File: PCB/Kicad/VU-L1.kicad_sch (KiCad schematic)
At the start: 32 parts, among them U1 SR1-L1, U2 SR2-L1

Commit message: PDF
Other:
- note added: "VU LINE 1"
- moved on the sheet: D16, D17, D18, D19, D20, D21, D22, D23, D24, D25, D26, D27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

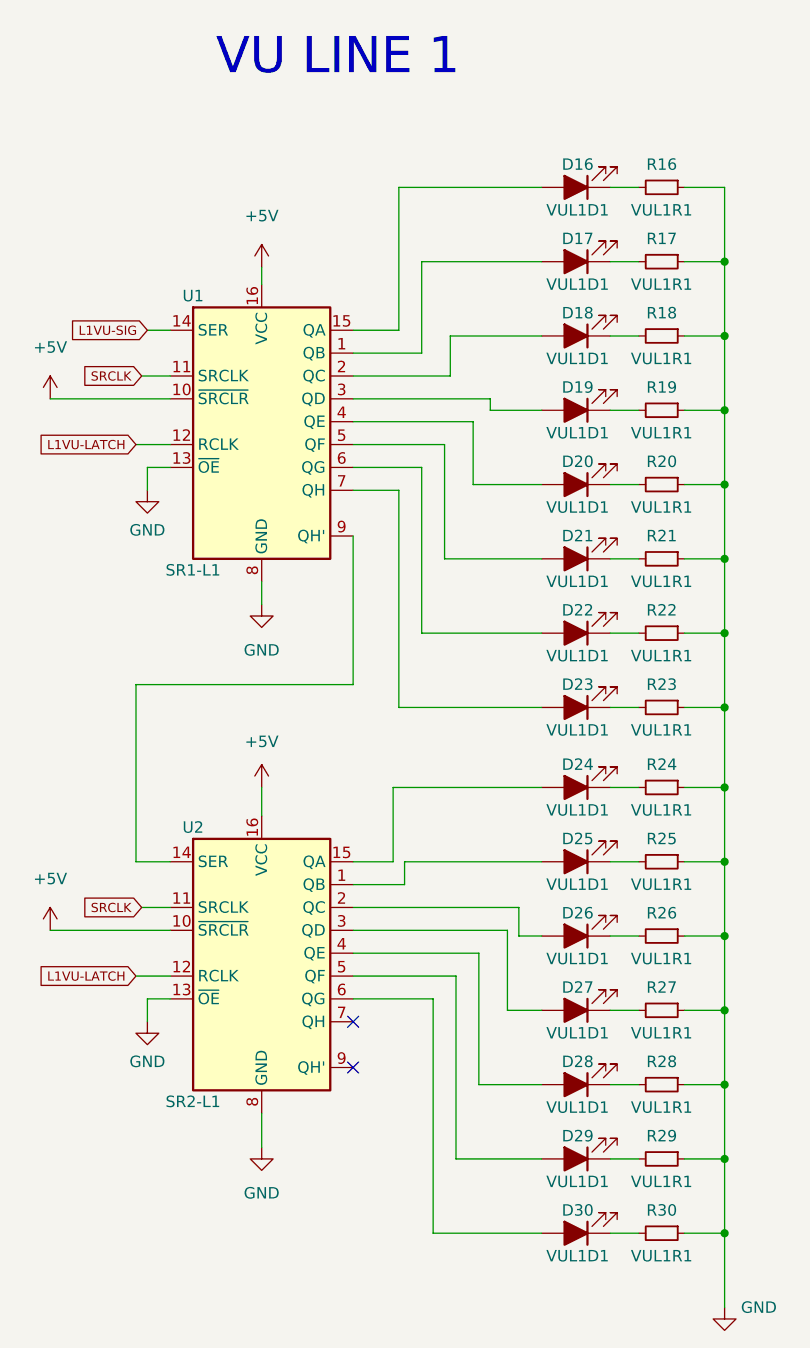
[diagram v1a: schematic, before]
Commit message: added transistor and 3x leds play- cue
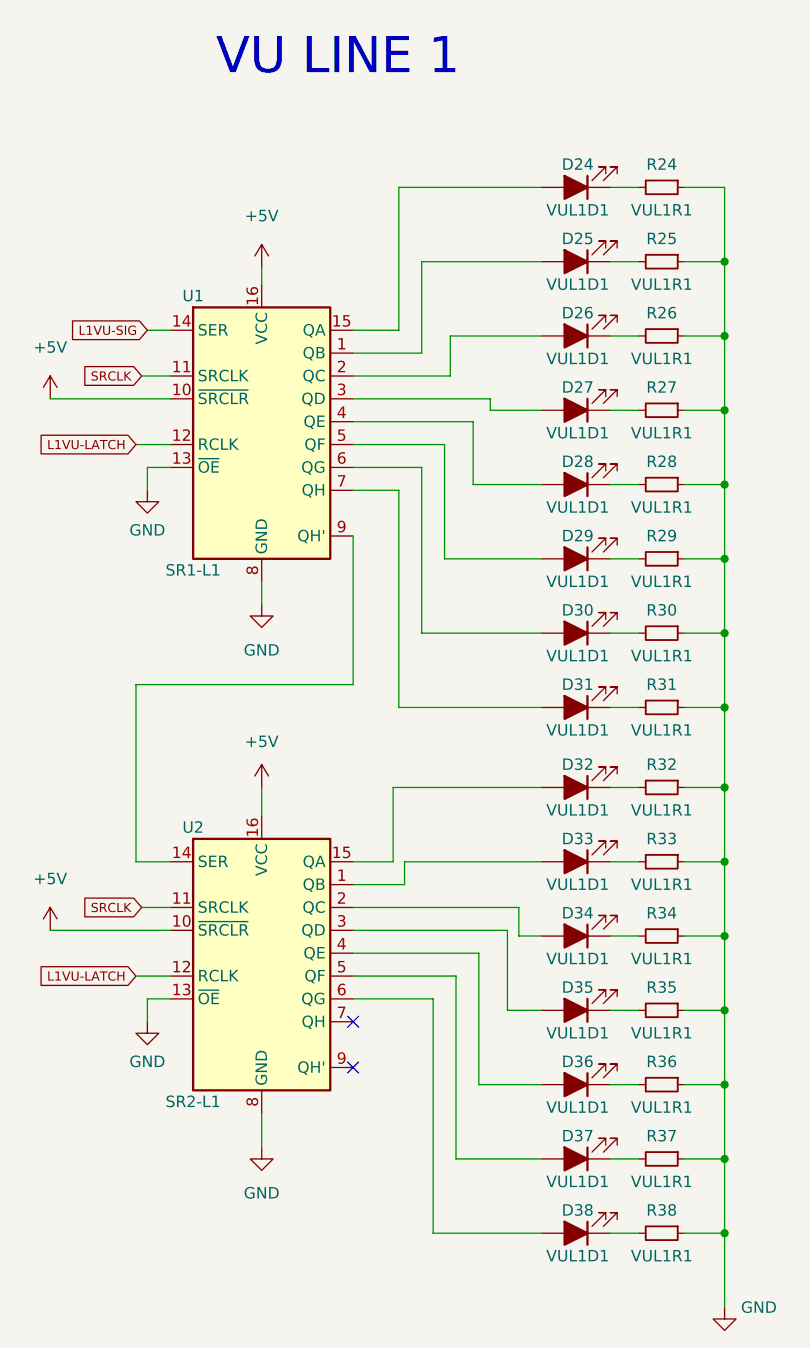
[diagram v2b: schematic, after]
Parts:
- U1, U2: footprint (none) -> Library:SO-16_3.9x9.9mm_P1.27mm
- renumbered D16 to D24, D17 to D25, D18 to D26, D19 to D27, D20 to D28, D21 to D29, D22 to D30, D23 to D31, D24 to D32, D25 to D33, D26 to D34, D27 to D35, D28 to D36, D29 to D37, D30 to D38, R16 to R24, R17 to R25, R18 to R26, R19 to R27, R20 to R28, R21 to R29, R22 to R30, R23 to R31, R24 to R32, R25 to R33, R26 to R34, R27 to R35, R28 to R36, R29 to R37, R30 to R38

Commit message: routing WIP
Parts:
- D33, D34, D35, D36: footprint Library:LED_GREEN -> Library:LED_YELLOW
- D37, D38: footprint Library:LED_GREEN -> Library:LED_RED
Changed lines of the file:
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@@
     (property "Reference" "D33" (id 0) (at 122.7455 115.57 0))
     (property "Value" "VUL1D1" (id 1) (at 122.7455 120.65 0))
-    (property "Footprint" "Library:LED_GREEN" (id 2) (at 122.555 118.11 0)
+    (property "Footprint" "Library:LED_YELLOW" (id 2) (at 122.555 118.11 0)
       (effects (font (size 1.27 1.27)) hide)
     )
@@
     (property "Reference" "D34" (id 0) (at 122.7455 123.825 0))
     (property "Value" "VUL1D1" (id 1) (at 122.7455 128.905 0))
-    (property "Footprint" "Library:LED_GREEN" (id 2) (at 122.555 126.365 0)
+    (property "Footprint" "Library:LED_YELLOW" (id 2) (at 122.555 126.365 0)
       (effects (font (size 1.27 1.27)) hide)
     )
@@
     (property "Reference" "D35" (id 0) (at 122.7455 132.08 0))
     (property "Value" "VUL1D1" (id 1) (at 122.7455 137.16 0))
-    (property "Footprint" "Library:LED_GREEN" (id 2) (at 122.555 134.62 0)
+    (property "Footprint" "Library:LED_YELLOW" (id 2) (at 122.555 134.62 0)
       (effects (font (size 1.27 1.27)) hide)
     )
@@
     (property "Reference" "D36" (id 0) (at 122.7455 140.335 0))
     (property "Value" "VUL1D1" (id 1) (at 122.7455 145.415 0))
-    (property "Footprint" "Library:LED_GREEN" (id 2) (at 122.555 142.875 0)
+    (property "Footprint" "Library:LED_YELLOW" (id 2) (at 122.555 142.875 0)
       (effects (font (size 1.27 1.27)) hide)
     )
@@
     (property "Reference" "D37" (id 0) (at 122.7455 148.59 0))
     (property "Value" "VUL1D1" (id 1) (at 122.7455 153.67 0))
-    (property "Footprint" "Library:LED_GREEN" (id 2) (at 122.555 151.13 0)
+    (property "Footprint" "Library:LED_RED" (id 2) (at 122.555 151.13 0)
       (effects (font (size 1.27 1.27)) hide)
     )
@@
     (property "Reference" "D38" (id 0) (at 122.7455 156.845 0))
     (property "Value" "VUL1D1" (id 1) (at 122.7455 161.925 0))
-    (property "Footprint" "Library:LED_GREEN" (id 2) (at 122.555 159.385 0)
+    (property "Footprint" "Library:LED_RED" (id 2) (at 122.555 159.385 0)
       (effects (font (size 1.27 1.27)) hide)
     )

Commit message: routes finished
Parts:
- D24, D25: footprint Library:LED_GREEN -> Library:LED_RED
- D26, D27, D28, D29: footprint Library:LED_GREEN -> Library:LED_YELLOW
- D33, D34, D35, D36: footprint Library:LED_YELLOW -> Library:LED_GREEN
- D37, D38: footprint Library:LED_RED -> Library:LED_GREEN
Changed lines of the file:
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@@
-(kicad_sch (version 20210615) (generator eeschema)
+(kicad_sch (version 20210621) (generator eeschema)
   (paper "A4")
   (junction (at 139.065 51.435) (diameter 0.9144) (color 0 0 0 0))
@@
     (property "Reference" "D24" (id 0) (at 122.7455 40.64 0))
     (property "Value" "VUL1D1" (id 1) (at 122.7455 45.72 0))
-    (property "Footprint" "Library:LED_GREEN" (id 2) (at 122.555 43.18 0)
+    (property "Footprint" "Library:LED_RED" (id 2) (at 122.555 43.18 0)
       (effects (font (size 1.27 1.27)) hide)
     )
@@
     (property "Reference" "D25" (id 0) (at 122.7455 48.895 0))
     (property "Value" "VUL1D1" (id 1) (at 122.7455 53.975 0))
-    (property "Footprint" "Library:LED_GREEN" (id 2) (at 122.555 51.435 0)
+    (property "Footprint" "Library:LED_RED" (id 2) (at 122.555 51.435 0)
       (effects (font (size 1.27 1.27)) hide)
     )
@@
     (property "Reference" "D26" (id 0) (at 122.7455 57.15 0))
     (property "Value" "VUL1D1" (id 1) (at 122.7455 62.23 0))
-    (property "Footprint" "Library:LED_GREEN" (id 2) (at 122.555 59.69 0)
+    (property "Footprint" "Library:LED_YELLOW" (id 2) (at 122.555 59.69 0)
       (effects (font (size 1.27 1.27)) hide)
     )
@@
     (property "Reference" "D27" (id 0) (at 122.7455 65.405 0))
     (property "Value" "VUL1D1" (id 1) (at 122.7455 70.485 0))
-    (property "Footprint" "Library:LED_GREEN" (id 2) (at 122.555 67.945 0)
+    (property "Footprint" "Library:LED_YELLOW" (id 2) (at 122.555 67.945 0)
       (effects (font (size 1.27 1.27)) hide)
     )
@@
     (property "Reference" "D28" (id 0) (at 122.7455 73.66 0))
     (property "Value" "VUL1D1" (id 1) (at 122.7455 78.74 0))
-    (property "Footprint" "Library:LED_GREEN" (id 2) (at 122.555 76.2 0)
+    (property "Footprint" "Library:LED_YELLOW" (id 2) (at 122.555 76.2 0)
       (effects (font (size 1.27 1.27)) hide)
     )
@@
     (property "Reference" "D29" (id 0) (at 122.7455 81.915 0))
     (property "Value" "VUL1D1" (id 1) (at 122.7455 86.995 0))
-    (property "Footprint" "Library:LED_GREEN" (id 2) (at 122.555 84.455 0)
+    (property "Footprint" "Library:LED_YELLOW" (id 2) (at 122.555 84.455 0)
       (effects (font (size 1.27 1.27)) hide)
     )
@@
     (property "Reference" "D33" (id 0) (at 122.7455 115.57 0))
     (property "Value" "VUL1D1" (id 1) (at 122.7455 120.65 0))
-    (property "Footprint" "Library:LED_YELLOW" (id 2) (at 122.555 118.11 0)
+    (property "Footprint" "Library:LED_GREEN" (id 2) (at 122.555 118.11 0)
       (effects (font (size 1.27 1.27)) hide)
     )
@@
     (property "Reference" "D34" (id 0) (at 122.7455 123.825 0))
     (property "Value" "VUL1D1" (id 1) (at 122.7455 128.905 0))
-    (property "Footprint" "Library:LED_YELLOW" (id 2) (at 122.555 126.365 0)
+    (property "Footprint" "Library:LED_GREEN" (id 2) (at 122.555 126.365 0)
       (effects (font (size 1.27 1.27)) hide)
     )
@@
     (property "Reference" "D35" (id 0) (at 122.7455 132.08 0))
     (property "Value" "VUL1D1" (id 1) (at 122.7455 137.16 0))
-    (property "Footprint" "Library:LED_YELLOW" (id 2) (at 122.555 134.62 0)
+    (property "Footprint" "Library:LED_GREEN" (id 2) (at 122.555 134.62 0)
       (effects (font (size 1.27 1.27)) hide)
     )
@@
     (property "Reference" "D36" (id 0) (at 122.7455 140.335 0))
     (property "Value" "VUL1D1" (id 1) (at 122.7455 145.415 0))
-    (property "Footprint" "Library:LED_YELLOW" (id 2) (at 122.555 142.875 0)
+    (property "Footprint" "Library:LED_GREEN" (id 2) (at 122.555 142.875 0)
       (effects (font (size 1.27 1.27)) hide)
     )
@@
     (property "Reference" "D37" (id 0) (at 122.7455 148.59 0))
     (property "Value" "VUL1D1" (id 1) (at 122.7455 153.67 0))
-    (property "Footprint" "Library:LED_RED" (id 2) (at 122.555 151.13 0)
+    (property "Footprint" "Library:LED_GREEN" (id 2) (at 122.555 151.13 0)
       (effects (font (size 1.27 1.27)) hide)
     )
@@
     (property "Reference" "D38" (id 0) (at 122.7455 156.845 0))
     (property "Value" "VUL1D1" (id 1) (at 122.7455 161.925 0))
-    (property "Footprint" "Library:LED_RED" (id 2) (at 122.555 159.385 0)
-      (effects (font (size 1.27 1.27)) hide)
-    )
+    (property "Footprint" "Library:LED_GREEN" (id 2) (at 122.555 159.385 0)
+      (effects (font (size 1.27 1.27)) hide)
+    )

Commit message: update schematic
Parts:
- R24, R25, R26, R27, R28, R29, R30, R31, R32, R33, R34, R35, R36, R37, R38: footprint Library:R_1206_3216Metric_Pad1.30x1.75mm_HandSolder -> Resistor_SMD:R_1206_3216Metric_Pad1.30x1.75mm_HandSolder
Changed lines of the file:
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@@
     (property "Reference" "R24" (id 0) (at 132.08 40.64 90))
     (property "Value" "VUL1R1" (id 1) (at 132.08 45.72 90))
-    (property "Footprint" "Library:R_1206_3216Metric_Pad1.30x1.75mm_HandSolder" (id 2) (at 132.08 43.18 0)
+    (property "Footprint" "Resistor_SMD:R_1206_3216Metric_Pad1.30x1.75mm_HandSolder" (id 2) (at 132.08 43.18 0)
       (effects (font (size 1.27 1.27)) hide)
     )
@@
     (property "Reference" "R25" (id 0) (at 132.08 48.895 90))
     (property "Value" "VUL1R1" (id 1) (at 132.08 53.975 90))
-    (property "Footprint" "Library:R_1206_3216Metric_Pad1.30x1.75mm_HandSolder" (id 2) (at 132.08 51.435 0)
+    (property "Footprint" "Resistor_SMD:R_1206_3216Metric_Pad1.30x1.75mm_HandSolder" (id 2) (at 132.08 51.435 0)
       (effects (font (size 1.27 1.27)) hide)
     )
@@
     (property "Reference" "R26" (id 0) (at 132.08 57.15 90))
     (property "Value" "VUL1R1" (id 1) (at 132.08 62.23 90))
-    (property "Footprint" "Library:R_1206_3216Metric_Pad1.30x1.75mm_HandSolder" (id 2) (at 132.08 59.69 0)
+    (property "Footprint" "Resistor_SMD:R_1206_3216Metric_Pad1.30x1.75mm_HandSolder" (id 2) (at 132.08 59.69 0)
       (effects (font (size 1.27 1.27)) hide)
     )
@@
     (property "Reference" "R27" (id 0) (at 132.08 65.405 90))
     (property "Value" "VUL1R1" (id 1) (at 132.08 70.485 90))
-    (property "Footprint" "Library:R_1206_3216Metric_Pad1.30x1.75mm_HandSolder" (id 2) (at 132.08 67.945 0)
+    (property "Footprint" "Resistor_SMD:R_1206_3216Metric_Pad1.30x1.75mm_HandSolder" (id 2) (at 132.08 67.945 0)
       (effects (font (size 1.27 1.27)) hide)
     )
@@
     (property "Reference" "R28" (id 0) (at 132.08 73.66 90))
     (property "Value" "VUL1R1" (id 1) (at 132.08 78.74 90))
-    (property "Footprint" "Library:R_1206_3216Metric_Pad1.30x1.75mm_HandSolder" (id 2) (at 132.08 76.2 0)
+    (property "Footprint" "Resistor_SMD:R_1206_3216Metric_Pad1.30x1.75mm_HandSolder" (id 2) (at 132.08 76.2 0)
       (effects (font (size 1.27 1.27)) hide)
     )
@@
     (property "Reference" "R29" (id 0) (at 132.08 81.915 90))
     (property "Value" "VUL1R1" (id 1) (at 132.08 86.995 90))
-    (property "Footprint" "Library:R_1206_3216Metric_Pad1.30x1.75mm_HandSolder" (id 2) (at 132.08 84.455 0)
+    (property "Footprint" "Resistor_SMD:R_1206_3216Metric_Pad1.30x1.75mm_HandSolder" (id 2) (at 132.08 84.455 0)
       (effects (font (size 1.27 1.27)) hide)
     )
@@
     (property "Reference" "R30" (id 0) (at 132.08 90.17 90))
     (property "Value" "VUL1R1" (id 1) (at 132.08 95.25 90))
-    (property "Footprint" "Library:R_1206_3216Metric_Pad1.30x1.75mm_HandSolder" (id 2) (at 132.08 92.71 0)
+    (property "Footprint" "Resistor_SMD:R_1206_3216Metric_Pad1.30x1.75mm_HandSolder" (id 2) (at 132.08 92.71 0)
       (effects (font (size 1.27 1.27)) hide)
     )
@@
     (property "Reference" "R31" (id 0) (at 132.08 98.425 90))
     (property "Value" "VUL1R1" (id 1) (at 132.08 103.505 90))
-    (property "Footprint" "Library:R_1206_3216Metric_Pad1.30x1.75mm_HandSolder" (id 2) (at 132.08 100.965 0)
+    (property "Footprint" "Resistor_SMD:R_1206_3216Metric_Pad1.30x1.75mm_HandSolder" (id 2) (at 132.08 100.965 0)
       (effects (font (size 1.27 1.27)) hide)
     )
@@
     (property "Reference" "R32" (id 0) (at 132.08 107.315 90))
     (property "Value" "VUL1R1" (id 1) (at 132.08 112.395 90))
-    (property "Footprint" "Library:R_1206_3216Metric_Pad1.30x1.75mm_HandSolder" (id 2) (at 132.08 109.855 0)
+    (property "Footprint" "Resistor_SMD:R_1206_3216Metric_Pad1.30x1.75mm_HandSolder" (id 2) (at 132.08 109.855 0)
       (effects (font (size 1.27 1.27)) hide)
     )
@@
     (property "Reference" "R33" (id 0) (at 132.08 115.57 90))
     (property "Value" "VUL1R1" (id 1) (at 132.08 120.65 90))
-    (property "Footprint" "Library:R_1206_3216Metric_Pad1.30x1.75mm_HandSolder" (id 2) (at 132.08 118.11 0)
+    (property "Footprint" "Resistor_SMD:R_1206_3216Metric_Pad1.30x1.75mm_HandSolder" (id 2) (at 132.08 118.11 0)
       (effects (font (size 1.27 1.27)) hide)
     )
@@
     (property "Reference" "R34" (id 0) (at 132.08 123.825 90))
     (property "Value" "VUL1R1" (id 1) (at 132.08 128.905 90))
-    (property "Footprint" "Library:R_1206_3216Metric_Pad1.30x1.75mm_HandSolder" (id 2) (at 132.08 126.365 0)
+    (property "Footprint" "Resistor_SMD:R_1206_3216Metric_Pad1.30x1.75mm_HandSolder" (id 2) (at 132.08 126.365 0)
       (effects (font (size 1.27 1.27)) hide)
     )
@@
     (property "Reference" "R35" (id 0) (at 132.08 132.08 90))
     (property "Value" "VUL1R1" (id 1) (at 132.08 137.16 90))
-    (property "Footprint" "Library:R_1206_3216Metric_Pad1.30x1.75mm_HandSolder" (id 2) (at 132.08 134.62 0)
+    (property "Footprint" "Resistor_SMD:R_1206_3216Metric_Pad1.30x1.75mm_HandSolder" (id 2) (at 132.08 134.62 0)
       (effects (font (size 1.27 1.27)) hide)
     )
@@
     (property "Reference" "R36" (id 0) (at 132.08 140.335 90))
     (property "Value" "VUL1R1" (id 1) (at 132.08 145.415 90))
-    (property "Footprint" "Library:R_1206_3216Metric_Pad1.30x1.75mm_HandSolder" (id 2) (at 132.08 142.875 0)
+    (property "Footprint" "Resistor_SMD:R_1206_3216Metric_Pad1.30x1.75mm_HandSolder" (id 2) (at 132.08 142.875 0)
       (effects (font (size 1.27 1.27)) hide)
     )
@@
     (property "Reference" "R37" (id 0) (at 132.08 148.59 90))
     (property "Value" "VUL1R1" (id 1) (at 132.08 153.67 90))
-    (property "Footprint" "Library:R_1206_3216Metric_Pad1.30x1.75mm_HandSolder" (id 2) (at 132.08 151.13 0)
+    (property "Footprint" "Resistor_SMD:R_1206_3216Metric_Pad1.30x1.75mm_HandSolder" (id 2) (at 132.08 151.13 0)
       (effects (font (size 1.27 1.27)) hide)
     )
@@
     (property "Reference" "R38" (id 0) (at 132.08 156.845 90))
     (property "Value" "VUL1R1" (id 1) (at 132.08 161.925 90))
-    (property "Footprint" "Library:R_1206_3216Metric_Pad1.30x1.75mm_HandSolder" (id 2) (at 132.08 159.385 0)
+    (property "Footprint" "Resistor_SMD:R_1206_3216Metric_Pad1.30x1.75mm_HandSolder" (id 2) (at 132.08 159.385 0)
       (effects (font (size 1.27 1.27)) hide)
     )

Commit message: modified trillbar connectors
Signed-off-by: Jose Vega <josevega234@gmail.com>
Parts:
- U1, U2: footprint Library:SO-16_3.9x9.9mm_P1.27mm -> Package_SO:SOIC-16_3.9x9.9mm_P1.27mm
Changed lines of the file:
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@@
-(kicad_sch (version 20210621) (generator eeschema)
+(kicad_sch (version 20210615) (generator eeschema)
   (paper "A4")
   (junction (at 139.065 51.435) (diameter 0.9144) (color 0 0 0 0))
@@
     (property "Reference" "U1" (id 0) (at 80.01 55.245 0))
     (property "Value" "SR1-L1" (id 1) (at 80.01 85.725 0))
-    (property "Footprint" "Library:SO-16_3.9x9.9mm_P1.27mm" (id 2) (at 87.63 69.215 0)
+    (property "Footprint" "Package_SO:SOIC-16_3.9x9.9mm_P1.27mm" (id 2) (at 87.63 69.215 0)
       (effects (font (size 1.27 1.27)) hide)
     )
@@
     (property "Reference" "U2" (id 0) (at 80.01 114.3 0))
     (property "Value" "SR2-L1" (id 1) (at 80.01 144.78 0))
-    (property "Footprint" "Library:SO-16_3.9x9.9mm_P1.27mm" (id 2) (at 87.63 128.27 0)
-      (effects (font (size 1.27 1.27)) hide)
-    )
+    (property "Footprint" "Package_SO:SOIC-16_3.9x9.9mm_P1.27mm" (id 2) (at 87.63 128.27 0)
+      (effects (font (size 1.27 1.27)) hide)
+    )
